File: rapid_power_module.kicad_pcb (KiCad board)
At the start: 4 copper layers, 80 x 136 mm, 200 parts, among them J1 Conn_02x04_Top_Bottom, J11 SWD Header, J12 SWD Header, J16 USB_C_Receptacle_USB2.0, J17 TC2050, J2 Conn_02x03_Odd_Even, J3 Conn_02x04_Top_Bottom, J4 Conn_02x03_Odd_Even, J5 Molex MicroFit 2x2, J6 Molex MicroFit 2x2, J7 Molex MicroFit 2x2, J8 Molex MicroFit 2x2, J9 Molex MicroFit 2x2, Q1 AOSP21321, Q12 AOSP21321, Q2 AOSP21321, Q3 AOSP21321, Q4 HiDRV1, Q5 LoDRV1, Q6 HiDRV2, Q7 LoDRV2, SW1 KMR721NGLFS, SW2 KMR721NGLFS, U1 BQ25756RRVR, U10 L7805, U11 MCP2562-E-SN, U12 STM32F105RCTx, U13 AZ1117I-3.3, U14 TPD4E1U06, U15 TPD4E1U06, U2 CYPD3177-24LQ, U3 BQ76952PFBR, Y3 8MHz 12pF

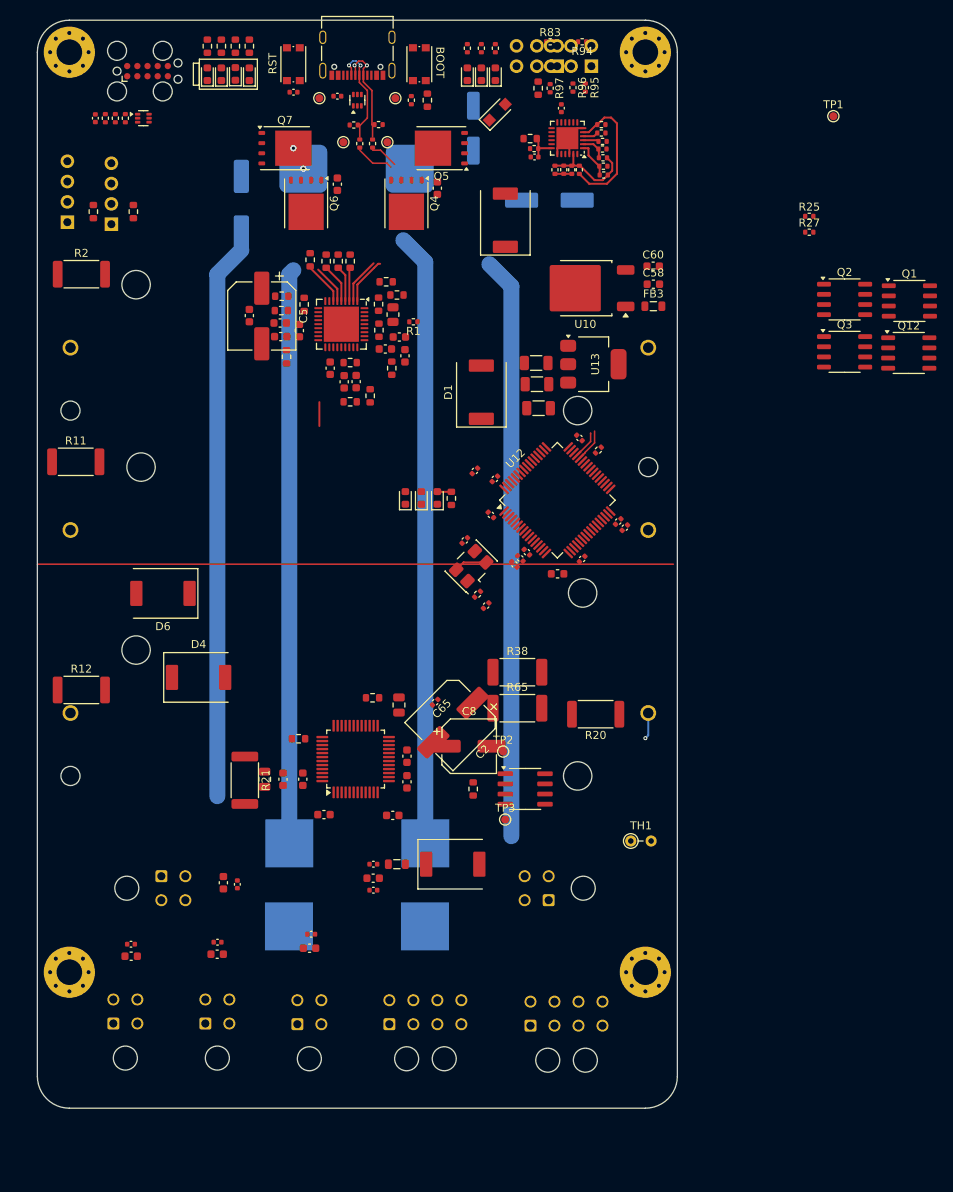
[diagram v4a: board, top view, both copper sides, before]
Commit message: Added footprints and LCSC
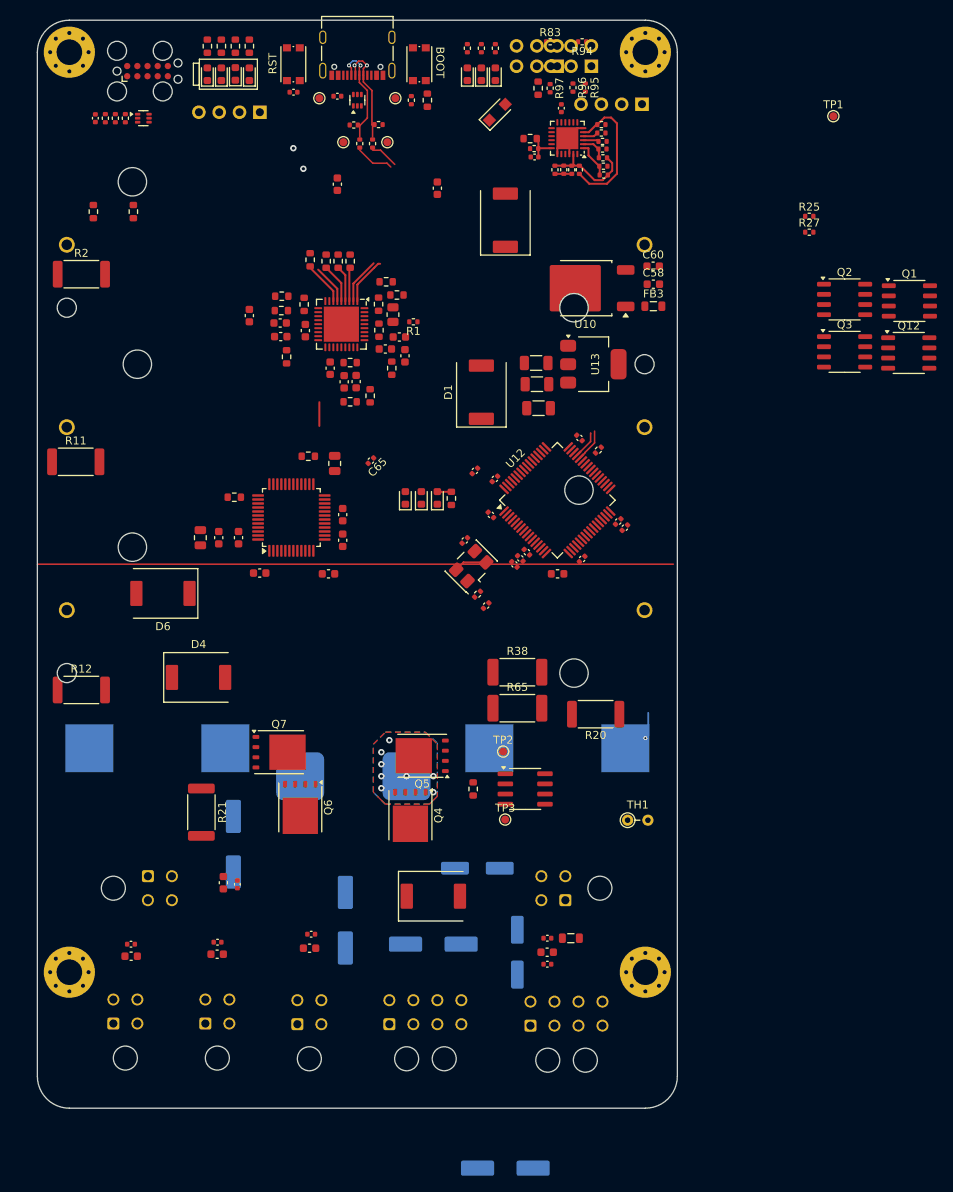
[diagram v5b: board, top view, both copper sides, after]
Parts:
- C2, C5, C8: moved to B.Cu
- moved C7 103.1 mm to (155.0, 138.5)
- moved C4 94.1 mm to (144.5, 137.5)
- moved C6 80.0 mm to (119.5, 125.0)
- moved Q4 76.5 mm to (141.6, 121.4)
- moved C5 76.2 mm to (133.5, 134.5)
- moved Q5 76.0 mm to (143.1, 114.0)
- moved L2 75.9 mm to (134.5, 116.5)
- moved Q6 75.5 mm to (127.9, 120.4)
- moved Q7 75.5 mm to (125.2, 113.5)
- moved J12 68.0 mm to (170.6, 32.5), turned to 90 degrees
- moved J7 58.6 mm to (161.0, 132.0), turned to 90 degrees
- moved J5 56.6 mm to (104.5, 147.4), turned to 0 degrees
- moved C2 56.1 mm to (153.5, 165.5), turned to 0 degrees
- moved F1 33.5 mm to (160.0, 113.0)
- moved C14 31.2 mm to (122.8, 91.1)
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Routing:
- net Net-(J5-Pin_3): track 76.5 -> 0.00 mm
- net PACK-: track 86.1 -> 13.3 mm, vias 1 -> 0
- net (no net): track 72.6 -> 0.00 mm
- net PACK+: track 71.9 -> 0.00 mm
- net Net-(J1-Pin_6): track 0.00 -> 3.30 mm, vias 0 -> 1
- net SW1: vias 0 -> 8
- added copper zone on B.Cu, net SW1
- added copper zone on F.Cu, net SW1

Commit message: fix diode and more routing work
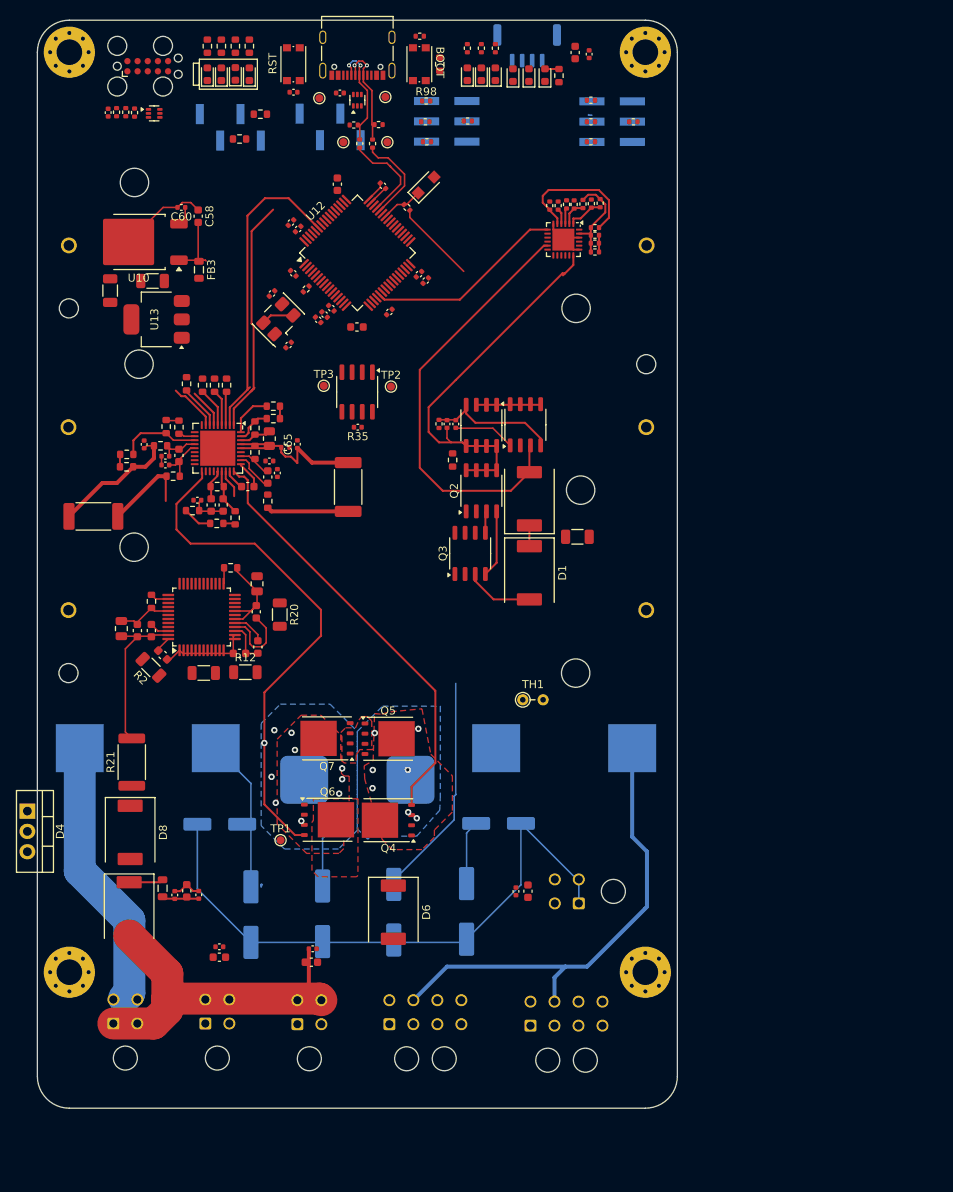
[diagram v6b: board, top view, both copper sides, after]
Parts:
- removed J9: Molex MicroFit 2x2, Connector_Molex:Molex_Micro-Fit_3.0_43045-0400_2x02_P3.00mm_Horizontal
- added D8: ~, Diode_SMD:ST_D_SMC, F.Cu at (106.6, 123.5)
- added J10: JST-GH 4Pin, Connector_JST:JST_GH_SM04B-GHS-TB_1x04-1MP_P1.25mm_Horizontal, B.Cu at (156.2, 25.2)
- added R28: 20k, Resistor_SMD:R_0603_1608Metric, F.Cu at (111.1, 72.8)
- added R29: 680, Resistor_SMD:R_0603_1608Metric, F.Cu at (114.4, 83.3)
- added R30: 49k9, Resistor_SMD:R_0603_1608Metric, F.Cu at (106.2, 76.3)
- C1, C3, C37, C38, C44, C45, C60: footprint Capacitor_SMD:C_0603_1608Metric -> Capacitor_SMD:C_0402_1005Metric
- D4: footprint Diode_SMD:ST_D_SMC -> Package_TO_SOT_THT:TO-220-3_Vertical
- J11, J12: footprint Connector_PinHeader_2.54mm:PinHeader_1x04_P2.54mm_Vertical -> Connector_PinHeader_2.54mm:PinHeader_1x04_P2.54mm_Vertical_SMD_Pin1Left
- J2, J4: footprint Connector_PinHeader_2.54mm:PinHeader_2x03_P2.54mm_Vertical -> Connector_PinHeader_2.54mm:PinHeader_2x03_P2.54mm_Vertical_SMD
- R11, R12, R2, R20: footprint Resistor_SMD:R_2512_6332Metric -> Resistor_SMD:R_1206_3216Metric
- R3: value 35k -> 15k
- R32: value 4k5 -> 4k7
- R35: footprint Resistor_SMD:R_0603_1608Metric -> Capacitor_SMD:C_0402_1005Metric
- R36: value 250k -> 200k
- R82: value 22k5 -> 22k
- R83: value 50k -> 49k9
- R96: value 5.1k -> 5k1
- R98: footprint Resistor_SMD:R_0603_1608Metric -> Resistor_SMD:R_0402_1005Metric
- moved C90 116.8 mm to (162.2, 26.0), turned to 90 degrees
- moved C91 115.4 mm to (164.0, 26.2), turned to 90 degrees
- moved TP1 113.9 mm to (125.4, 124.5)
- moved C60 59.4 mm to (113.0, 45.4), turned to 180 degrees
- moved TP3 58.8 mm to (130.8, 67.7)
- moved C58 57.5 mm to (115.1, 46.5), turned to -90 degrees
- moved FB3 57.0 mm to (115.2, 53.2), turned to -90 degrees
- moved R38 56.5 mm to (102.0, 84.0), turned to 180 degrees
- moved U10 56.1 mm to (107.7, 49.7)
- moved U13 54.9 mm to (109.9, 59.4), turned to 180 degrees
- moved R69 54.5 mm to (160.2, 28.9)
- moved D20 54.5 mm to (154.4, 28.9)
- moved D21 54.5 mm to (156.4, 28.9)
- moved D22 54.5 mm to (158.4, 28.9)
- moved Q12 54.2 mm to (150.5, 72.7), turned to -90 degrees
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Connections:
- C90 pad 1: +VSW -> PACK+
- C91 pad 1: +VSW -> PACK+
- R21 pad 1: Net-(D4-K) -> Net-(D8-K)
- R3 pad 2: Net-(U1-FB) -> Net-(R28-Pad1)
- R36 pad 1: Net-(U1-FB) -> Net-(R30-Pad2)
- R82 pad 2: PACK- -> Net-(R29-Pad1)
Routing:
- net PACK-: track 13.3 -> 136.2 mm
- net HIDRV2: track 0.00 -> 64.5 mm, vias 0 -> 1
- net USB_PD_OUT: track 0.00 -> 61.6 mm
- net Net-(J1-Pin_6): track 3.30 -> 61.6 mm, vias 1 -> 0
- net /VBUS: track 4.07 -> 58.7 mm
- net HIDRV1: track 0.00 -> 53.8 mm
- net VAC: track 0.00 -> 52.1 mm
- net +VSW: track 0.00 -> 48.1 mm
- net Net-(J5-Pin_3): track 0.00 -> 37.1 mm
- net PACK+: track 0.00 -> 36.1 mm
- net I2C_SDA: track 5.78 -> 38.8 mm
- net USB_PD_INTERRUPT: track 0.00 -> 24.9 mm
- net I2C_SCL: track 5.99 -> 29.7 mm
- net BuckBoostOut: track 0.00 -> 19.9 mm
- net Net-(U3-BAT): track 0.00 -> 19.6 mm
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- added copper zone on F.Cu, net BuckBoostOut
- added copper zone on F.Cu, net PACK-
- added copper zone on B.Cu, net SW2
- added copper zone on F.Cu, net SW2
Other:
- board text added: "PW"
- board text added: "PW SPCB"
- board text added: "VB"

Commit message: more routing work
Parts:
- removed R92, R93: 0R, Resistor_SMD:R_0402_1005Metric
- added C20: 1u, Capacitor_SMD:C_0402_1005Metric, F.Cu at (164.0, 47.0)
- added R39: 4.7k, Resistor_SMD:R_0603_1608Metric, F.Cu at (156.0, 50.8)
- added R40: 10k, Resistor_SMD:R_0603_1608Metric, F.Cu at (156.0, 49.2)
- added R42: 10k, Resistor_SMD:R_0603_1608Metric, F.Cu at (156.0, 47.8)
- TH1, TP1: moved to B.Cu
- moved R38 52.2 mm to (126.3, 130.2)
- moved BT1 45.1 mm to (135.0, 95.2)
- moved BT3 44.3 mm to (135.0, 51.4)
- moved C46 43.7 mm to (112.1, 81.2)
- moved TP3 10.6 mm to (138.8, 60.8)
- moved R35 8.68 mm to (135.0, 64.2), turned to 0 degrees
- moved TP2 6.52 mm to (135.7, 62.3), turned to 45 degrees
- moved R21 5.81 mm to (101.0, 115.0)
- moved D8 5.51 mm to (108.0, 118.2), turned to 0 degrees
- moved R88 5.45 mm to (111.5, 33.7)
- moved C83 4.55 mm to (112.1, 128.0), turned to -90 degrees
- moved C81 4.48 mm to (115.1, 128.0), turned to -90 degrees
- moved TP1 4.22 mm to (126.4, 128.6), turned to 180 degrees
- moved C77 3.77 mm to (122.7, 61.9), turned to 135 degrees
- moved R26 3.66 mm to (152.4, 25.8)
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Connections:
- U12 pad 2: STAT_LED0 -> unconnected-(U12-PC13-Pad2)
- U12 pad 21: USB_PD_INTERRUPT -> unconnected-(U12-PA5-Pad21)
- U12 pad 25: INT -> unconnected-(U12-PC5-Pad25)
- U12 pad 26: unconnected-(U12-PB0-Pad26) -> FLIP
- U12 pad 27: unconnected-(U12-PB1-Pad27) -> FAULT
- U12 pad 28: unconnected-(U12-PB2-Pad28) -> GPIO_1
- U12 pad 29: unconnected-(U12-PB10-Pad29) -> USB_PD_INTERRUPT
- U12 pad 3: STAT_LED1 -> unconnected-(U12-PC14-Pad3)
- U12 pad 33: CHRG_IND_LED_1 -> STAT_LED0
- U12 pad 34: CHRG_IND_LED_2 -> STAT_LED1
- U12 pad 35: CHRG_IND_LED_3 -> STAT_LED2
- U12 pad 36: CHRG_IND_LED_4 -> PG
- U12 pad 39: PG -> unconnected-(U12-PC8-Pad39)
- U12 pad 4: STAT_LED2 -> unconnected-(U12-PC15-Pad4)
- U12 pad 51: unconnected-(U12-PC10-Pad51) -> INT
- U12 pad 54: unconnected-(U12-PD2-Pad54) -> CHRG_IND_LED_1
- U12 pad 55: unconnected-(U12-PB3-Pad55) -> CHRG_IND_LED_2
- U12 pad 56: unconnected-(U12-PB4-Pad56) -> CHRG_IND_LED_3
- U12 pad 57: unconnected-(U12-PB5-Pad57) -> CHRG_IND_LED_4
- U14 pad 4: Net-(U14-IO3) -> /D0-
- U14 pad 5: Net-(U14-IO4) -> /D0+
- U2 pad 10: unconnected-(U2-FLIP-Pad10) -> FLIP
- U2 pad 24: unconnected-(U2-VCCD-Pad24) -> Net-(U2-VCCD)
- U2 pad 8: unconnected-(U2-GPIO_1-Pad8) -> GPIO_1
- U2 pad 9: unconnected-(U2-FAULT-Pad9) -> FAULT
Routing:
- net PACK+: track 36.1 -> 134.7 mm, vias 0 -> 10
- net Net-(D4-K): track 0.00 -> 91.2 mm
- net main_voltage: track 4.63 -> 87.7 mm, vias 0 -> 3
- net CC2: track 0.00 -> 73.5 mm, vias 0 -> 4
- net /VBUS: track 58.7 -> 121.3 mm
- net CC1: track 0.00 -> 61.3 mm, vias 0 -> 2
- net BuckBoostOut: track 19.9 -> 80.1 mm, vias 0 -> 7
- net SWCLK: track 0.00 -> 45.6 mm, vias 0 -> 1
- net NRST: track 0.00 -> 43.7 mm
- net VAC: track 52.1 -> 95.1 mm, vias 0 -> 3
- net INT: track 4.20 -> 42.9 mm
- net CHRG_IND_LED_4: track 0.00 -> 37.1 mm, vias 0 -> 2
- net CHRG_IND_LED_2: track 0.00 -> 35.1 mm, vias 0 -> 3
- net CHRG_IND_LED_3: track 0.00 -> 34.4 mm, vias 0 -> 2
- net LODRV1: track 3.55 -> 35.5 mm, vias 0 -> 2
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- added copper zone on B.Cu, net BuckBoostOut
- added copper zone on F.Cu, net Net-(Q1-G)
- added copper zone on B.Cu, net PACK+
- added copper zone on F.Cu, net PACK+
- added copper zone on F.Cu, net main_voltage

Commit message: more routing
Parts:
- D4: footprint Package_TO_SOT_THT:TO-220-3_Vertical -> Diode_SMD:D_SOD-323
- moved D4 116.7 mm to (163.9, 27.7), turned to 0 degrees
- moved R65 50.7 mm to (143.9, 130.0), turned to 0 degrees
- moved TH1 32.8 mm to (133.7, 84.2), turned to 0 degrees
- moved C91 3.03 mm to (166.3, 25.1)
- moved C90 2.83 mm to (164.8, 25.1)
- moved D6 1.80 mm to (139.3, 136.5)
- moved C78 1.63 mm to (123.3, 57.5)
- moved BT1 1.21 mm to (133.9, 95.8)
- moved TP7 0.91 mm to (137.9, 32.3)
- moved TP6 0.89 mm to (129.8, 30.9)
- moved R91 0.58 mm to (114.2, 67.6)
- moved R74 0.57 mm to (129.0, 56.0)
- moved C23 0.43 mm to (132.6, 31.5), turned to 90 degrees
- moved BT2 0.32 mm to (135.0, 72.5)
- moved R96 0.10 mm to (164.2, 32.1)
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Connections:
- U12 pad 16: RST_SHUT -> unconnected-(U12-PA2-Pad16)
- U12 pad 2: unconnected-(U12-PC13-Pad2) -> RST_SHUT
- U12 pad 3: unconnected-(U12-PC14-Pad3) -> REGIN
- U12 pad 4: unconnected-(U12-PC15-Pad4) -> BREG
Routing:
- net PACK+: track 134.7 -> 269.6 mm, vias 10 -> 11
- net CAN-: track 9.02 -> 123.1 mm
- net CAN+: track 8.83 -> 119.6 mm
- net Net-(Q2-G): track 8.41 -> 90.9 mm, vias 0 -> 6
- net I2C_SCL: track 49.4 -> 129.9 mm, vias 3 -> 10
- net Net-(J2-Pin_2): track 0.00 -> 79.0 mm, vias 0 -> 2
- net Net-(D4-K): track 91.2 -> 13.3 mm, vias 0 -> 1
- net I2C_SDA: track 43.5 -> 118.8 mm, vias 1 -> 9
- net RST_SHUT: track 0.00 -> 68.3 mm, vias 0 -> 4
- net Net-(Q4-D): track 18.3 -> 81.8 mm, vias 0 -> 1
- net REGIN: track 0.00 -> 63.3 mm, vias 0 -> 4
- net BREG: track 0.00 -> 61.2 mm, vias 0 -> 4
- net Net-(Q1-G): track 4.57 -> 62.6 mm, vias 0 -> 2
- net TS2: track 0.00 -> 56.4 mm, vias 0 -> 2
- net BAL_ALERT: track 2.01 -> 56.7 mm, vias 0 -> 4
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- added copper zone on F.Cu, net /VBUS
- added copper zone on F.Cu, net Net-(Q2-S-Pad1)
- added copper zone on F.Cu, net SAFE_PWR_OUT
